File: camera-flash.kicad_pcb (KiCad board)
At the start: 2 copper layers, 100 x 95.8 mm, 94 parts, among them J1 USB, J10 CAM, J11 GND, J2 LED_WW_A, J3 LED_WW_C, J4 LED_CW_A, J5 LED_CW_C, J6 IN, J7 OUT, J8 CAM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

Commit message: routing 50% done"
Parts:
- D1, D2, D5: footprint Diode_SMD:D_SMA -> Diode_SMD:D_SOD-123F
- Q1, Q2: value 2N7002 -> ONSC-NMOS-8_E; footprint Package_TO_SOT_SMD:SOT-23 -> Package_SO:SO-8_3.9x4.9mm_P1.27mm
- R10, R9: footprint otter:R_0603 -> otter:R_0805
- moved C19 204.0 mm to (119.9, 126.8), turned to 90 degrees
- moved R27 203.2 mm to (135.4, 100.3), turned to 225 degrees
- moved C20 202.8 mm to (137.3, 106.2), turned to 270 degrees
- moved U7 198.6 mm to (132.6, 105.0)
- moved R13 193.0 mm to (113.1, 138.0), turned to 270 degrees
- moved C21 190.0 mm to (128.0, 103.7), turned to 270 degrees
- moved R16 189.6 mm to (128.1, 101.5), turned to 180 degrees
- moved R17 188.9 mm to (128.0, 106.2), turned to 270 degrees
- moved R14 187.0 mm to (120.5, 128.8), turned to 180 degrees
- moved D5 186.4 mm to (109.9, 126.8), turned to 90 degrees
- moved C23 186.0 mm to (133.7, 108.6), turned to 180 degrees
- moved R18 185.6 mm to (130.6, 108.5)
- moved C22 184.4 mm to (125.0, 123.3), turned to 90 degrees
- moved U5 183.8 mm to (115.2, 126.8), turned to 90 degrees
- moved U6 182.7 mm to (122.5, 124.3)
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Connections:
- J6 pad 1: Net-(D5-Pad2) -> Net-(J6-Pad1)
- J6 pad 2: Net-(J6-Pad2) -> Net-(D5-Pad2)
- Q1 pad 1: Net-(Q1-Pad1) -> Net-(C17-Pad1)
- Q1 pad 3: Net-(C17-Pad2) -> Net-(C17-Pad1)
- Q2 pad 1: Net-(Q2-Pad1) -> Net-(C18-Pad1)
- Q2 pad 3: Net-(C18-Pad2) -> Net-(C18-Pad1)
- R12 pad 2: WW_DIM -> CW_DIM
- R13 pad 2: Net-(J6-Pad2) -> Net-(J6-Pad1)
- R19 pad 1: Net-(Q1-Pad1) -> Net-(Q1-Pad4)
- R20 pad 1: Net-(Q2-Pad1) -> Net-(Q2-Pad4)
- R8 pad 1: WW_DIM -> CW_DIM
- U4 pad 6: WW_DIM -> CW_DIM
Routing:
- net CC2: track 0.00 -> 4.70 mm
- net CC1: track 0.00 -> 4.28 mm
- added copper zone on B.Cu, net GND
- added copper zone on F.Cu, net GND

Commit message: update
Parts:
- moved D1 102.5 mm to (126.3, 62.6), turned to 135 degrees
- moved R19 90.2 mm to (123.0, 59.5), turned to 135 degrees
- moved C24 89.5 mm to (101.5, 55.5)
- moved Q3 89.1 mm to (101.5, 53.0), turned to 180 degrees
- moved R23 85.7 mm to (98.5, 53.5), turned to 180 degrees
- moved Q7 85.6 mm to (95.5, 53.5), turned to 90 degrees
- moved R21 85.4 mm to (98.5, 52.0), turned to 180 degrees
- moved Q4 77.1 mm to (105.0, 53.0), turned to 270 degrees
- moved D2 74.3 mm to (72.0, 106.0), turned to 90 degrees
- moved R25 69.4 mm to (98.5, 55.0)
- moved C25 48.8 mm to (74.0, 94.1), turned to 90 degrees
- moved Q5 45.4 mm to (72.3, 97.4), turned to 90 degrees
- moved C12 45.1 mm to (61.3, 116.0), turned to 270 degrees
- moved R24 40.1 mm to (72.4, 94.4), turned to 90 degrees
- moved R20 39.3 mm to (70.5, 100.8), turned to 90 degrees
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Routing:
- net +3V3: track 0.00 -> 234.3 mm, vias 0 -> 6
- net Net-(C17-Pad2): track 0.00 -> 26.5 mm
- net Net-(C18-Pad2): track 0.00 -> 25.3 mm
- net Net-(D5-Pad2): track 0.00 -> 23.4 mm
- net Net-(C18-Pad1): track 0.00 -> 22.3 mm
- net VBUS: track 0.00 -> 18.9 mm, vias 0 -> 15
- net GND: track 0.00 -> 16.3 mm
- net Net-(D5-Pad1): track 0.00 -> 12.7 mm
- net Net-(SW3-Pad3): track 0.00 -> 12.6 mm
- net Net-(SW2-Pad2): track 0.00 -> 12.2 mm
- net Net-(C17-Pad1): track 0.00 -> 11.5 mm
- net Net-(R14-Pad1): track 0.00 -> 10.7 mm
- net Net-(SW3-Pad2): track 0.00 -> 8.27 mm
- net flash_in: track 0.00 -> 8.14 mm
- net Net-(R15-Pad1): track 0.00 -> 7.65 mm
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- added copper zone on B.Cu, net Net-(C13-Pad1)
- added copper zone on B.Cu, net Net-(C14-Pad1)
- added copper zone on B.Cu, net Net-(C17-Pad1)
- added copper zone on B.Cu, net Net-(C17-Pad2)
- added copper zone on B.Cu, net Net-(C18-Pad1)
- added copper zone on B.Cu, net Net-(C18-Pad2)
- added copper zone on B.Cu, net VBUS
- added copper zone on F.Cu, net VBUS
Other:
- rule pad_to_mask_clearance: 0.051 -> 0

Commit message: update
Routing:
- net VBUS: track 18.9 -> 244.8 mm, vias 15 -> 30
- net flash_pulse: track 3.29 -> 172.9 mm, vias 0 -> 9
- net flash_in: track 8.14 -> 71.4 mm, vias 0 -> 6
- net +3V3: track 234.3 -> 295.7 mm, vias 6 -> 10
- net Net-(R12-Pad1): track 0.00 -> 42.7 mm, vias 0 -> 2
- net Net-(Q3-Pad2): track 0.00 -> 23.5 mm
- net Net-(R11-Pad1): track 0.00 -> 12.1 mm, vias 0 -> 2
- net Net-(R15-Pad1): track 7.65 -> 14.1 mm, vias 0 -> 2
- net Net-(Q7-Pad3): track 0.00 -> 6.12 mm
- net Net-(Q3-Pad1): track 0.00 -> 4.80 mm
- net Net-(Q5-Pad2): track 3.06 -> 6.24 mm
- net Net-(Q1-Pad4): track 0.00 -> 2.39 mm
- net Net-(Q8-Pad1): track 6.64 -> 4.32 mm
- net Net-(Q5-Pad1): track 5.14 -> 7.41 mm
- net Net-(Q7-Pad1): track 0.00 -> 1.51 mm
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
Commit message: update
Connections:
- J1 pad A6: D+ -> Net-(J1-PadA6)
- J1 pad A7: D- -> Net-(J1-PadA7)
- J1 pad B6: D+ -> Net-(J1-PadB6)
- J1 pad B7: D- -> Net-(J1-PadB7)
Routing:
- net GND: vias 7 -> 135
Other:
- net class Default: clearance 0.2 -> 0.19
- rule trace_clearance: 0.2 -> 0.19

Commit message: update
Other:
- board text added: "CW"
- board text added: "DELAY"
- board text added: "DELAYED DIRECT"
- board text added: "IN - +"
- board text added: "OFF ON"
- board text added: "OUT + -"
- board text added: "OUTPUT"
- board text added: "T-ON"
- board text added: "TRIGGER"
- board text added: "WW"
- board text added: "↑ ↓"
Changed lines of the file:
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@@
   (general
     (thickness 1.6)
-    (drawings 9)
+    (drawings 29)
     (tracks 709)
     (zones 0)
@@
     (pcbplotparams
       (layerselection 0x010fc_ffffffff)
-      (usegerberextensions false)
+      (usegerberextensions true)
       (usegerberattributes false)
       (usegerberadvancedattributes false)
@@
       (psa4output false)
       (plotreference true)
-      (plotvalue true)
+      (plotvalue false)
       (plotinvisibletext false)
       (padsonsilk false)
@@
       (outputformat 1)
       (mirror false)
-      (drillshape 1)
+      (drillshape 0)
       (scaleselection 1)
-      (outputdirectory ""))
+      (outputdirectory "gerber/"))
   )
   (net 0 "")
@@
     )
   )
+  (gr_line (start 114.4 141.6) (end 110.6 141.6) (layer F.SilkS) (width 0.12))
+  (gr_line (start 110.6 145.4) (end 114.4 145.4) (layer F.SilkS) (width 0.12))
+  (gr_line (start 110.6 141.6) (end 110.6 145.4) (layer F.SilkS) (width 0.12))
+  (gr_line (start 114.4 145.4) (end 114.4 141.6) (layer F.SilkS) (width 0.12))
+  (gr_line (start 89.4 141.6) (end 85.6 141.6) (layer F.SilkS) (width 0.12))
+  (gr_line (start 89.4 145.4) (end 89.4 141.6) (layer F.SilkS) (width 0.12))
+  (gr_line (start 85.6 145.4) (end 89.4 145.4) (layer F.SilkS) (width 0.12))
+  (gr_line (start 85.6 141.6) (end 85.6 145.4) (layer F.SilkS) (width 0.12))
+  (gr_text "DELAYED  DIRECT\n" (at 88 137.8) (layer F.SilkS)
+    (effects (font (size 0.8 0.8) (thickness 0.15)))
+  )
+  (gr_text OUTPUT (at 88.2 131.4) (layer F.SilkS)
+    (effects (font (size 1 1) (thickness 0.15)))
+  )
+  (gr_text CW (at 71.4 64.8) (layer F.SilkS)
+    (effects (font (size 1 1) (thickness 0.15)))
+  )
+  (gr_text "WW\n" (at 134.2 79.8) (layer F.SilkS)
+    (effects (font (size 1 1) (thickness 0.15)))
+  )
+  (gr_text T-ON (at 130 86.2) (layer F.SilkS)
+    (effects (font (size 1 1) (thickness 0.15)))
+  )
+  (gr_text DELAY (at 140.6 106.6) (layer F.SilkS)
+    (effects (font (size 1 1) (thickness 0.15)))
+  )
+  (gr_text "↑   ↓" (at 131.8 129.4) (layer F.SilkS)
+    (effects (font (size 1 1) (thickness 0.15)))
+  )
+  (gr_text "OFF ON" (at 142 101) (layer F.SilkS)
+    (effects (font (size 1 1) (thickness 0.15)))
+  )
+  (gr_text DELAY (at 142 94.8) (layer F.SilkS)
+    (effects (font (size 1 1) (thickness 0.15)))
+  )
+  (gr_text TRIGGER (at 131.8 123.2) (layer F.SilkS)
+    (effects (font (size 1 1) (thickness 0.15)))
+  )
+  (gr_text "OUT\n+ -" (at 87.4 143.5) (layer F.SilkS)
+    (effects (font (size 1 1) (thickness 0.15)))
+  )
+  (gr_text "IN\n- +" (at 112.4 143.5) (layer F.SilkS)
+    (effects (font (size 1 1) (thickness 0.15)))
+  )
   (gr_line (start 100 136) (end 100 126.1) (layer Eco2.User) (width 0.15))
   (gr_text "PD OK\n" (at 99.3 128) (layer F.SilkS)
@@
   (gr_line (start 120.06 145.8) (end 79.94 145.8) (layer Edge.Cuts) (width 0.05))
   (gr_circle (center 100 100) (end 125 100) (layer Edge.Cuts) (width 0.05))
+  (segment (start 102.95 131.4) (end 103.45 131.4) (width 0.2) (layer B.Cu) (net 1))
+  (segment (start 102.8 131.55) (end 102.95 131.4) (width 0.2) (layer B.Cu) (net 1))
+  (segment (start 102.8 132.325) (end 102.8 131.55) (width 0.2) (layer B.Cu) (net 1))
+  (segment (start 102.575 132.55) (end 102.8 132.325) (width 0.2) (layer B.Cu) (net 1))
+  (segment (start 101.9625 132.55) (end 102.575 132.55) (width 0.2) (layer B.Cu) (net 1))
   (via (at 116.25 70.75) (size 0.6) (drill 0.3) (layers F.Cu B.Cu) (net 2))
   (via (at 110.25 133) (size 0.6) (drill 0.3) (layers F.Cu B.Cu) (net 2))
@@
   (via (at 100.75 133.5) (size 0.6) (drill 0.3) (layers F.Cu B.Cu) (net 2))
   (via (at 100.75 132) (size 0.6) (drill 0.3) (layers F.Cu B.Cu) (net 2))
-  (via (at 102.1 137.1) (size 0.6) (drill 0.3) (layers F.Cu B.Cu) (net 5))
-  (via (at 102.1 136.4) (size 0.6) (drill 0.3) (layers F.Cu B.Cu) (net 5))
-  (segment (start 102.95 131.4) (end 103.45 131.4) (width 0.2) (layer B.Cu) (net 1))
-  (segment (start 102.8 131.55) (end 102.95 131.4) (width 0.2) (layer B.Cu) (net 1))
-  (segment (start 102.8 132.325) (end 102.8 131.55) (width 0.2) (layer B.Cu) (net 1))
-  (segment (start 102.575 132.55) (end 102.8 132.325) (width 0.2) (layer B.Cu) (net 1))
-  (segment (start 101.9625 132.55) (end 102.575 132.55) (width 0.2) (layer B.Cu) (net 1))
   (segment (start 114.927565 68.177565) (end 114.927565 69.322435) (width 0.25) (layer B.Cu) (net 2))
   (segment (start 114.132159 67.382159) (end 114.927565 68.177565) (width 0.25) (layer B.Cu) (net 2))
@@
   (segment (start 72 110) (end 73.75 108.25) (width 0.2) (layer B.Cu) (net 4))
   (segment (start 66.5 119.25) (end 66.625 119.25) (width 0.2) (layer B.Cu) (net 4))
+  (via (at 102.1 137.1) (size 0.6) (drill 0.3) (layers F.Cu B.Cu) (net 5))
+  (via (at 102.1 136.4) (size 0.6) (drill 0.3) (layers F.Cu B.Cu) (net 5))
   (segment (start 116.447845 73.508505) (end 117.56967 74.63033) (width 0.25) (layer B.Cu) (net 5))
   (segment (start 116.447845 73.392566) (end 116.447845 73.508505) (width 0.25) (layer B.Cu) (net 5))

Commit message: finished layout
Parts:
- moved RV2 4.28 mm to (74.1, 73.3)
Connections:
- RV2 pad 1: Net-(RV2-Pad1) -> +3V3
- RV2 pad 2: +3V3 -> Net-(R12-Pad1)
- RV2 pad 3: Net-(R12-Pad1) -> Net-(RV2-Pad3)
- RV4 pad 2: +3V3 -> Net-(R16-Pad1)
- RV4 pad 3: Net-(R16-Pad1) -> +3V3
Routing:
- net +3V3: track 295.7 -> 242.8 mm
- net VBUS: track 244.8 -> 271.5 mm
- net Net-(R11-Pad1): track 12.1 -> 14.9 mm
- net Net-(R12-Pad1): track 42.7 -> 43.9 mm
- net Net-(R15-Pad1): track 14.1 -> 13.1 mm, vias 2 -> 0
- net GND: vias 135 -> 137
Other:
- board text added: "+ -"
- board text added: "BRIGHTNESS CW"
- board text added: "BRIGHTNESS WW"
- board text added: "Jan Henrik 2020"
- board text added: "Zoetrope -Flash"
- board text added: "t-ON"
- board text removed: "CW"
- board text removed: "T-ON"
- board text removed: "WW"

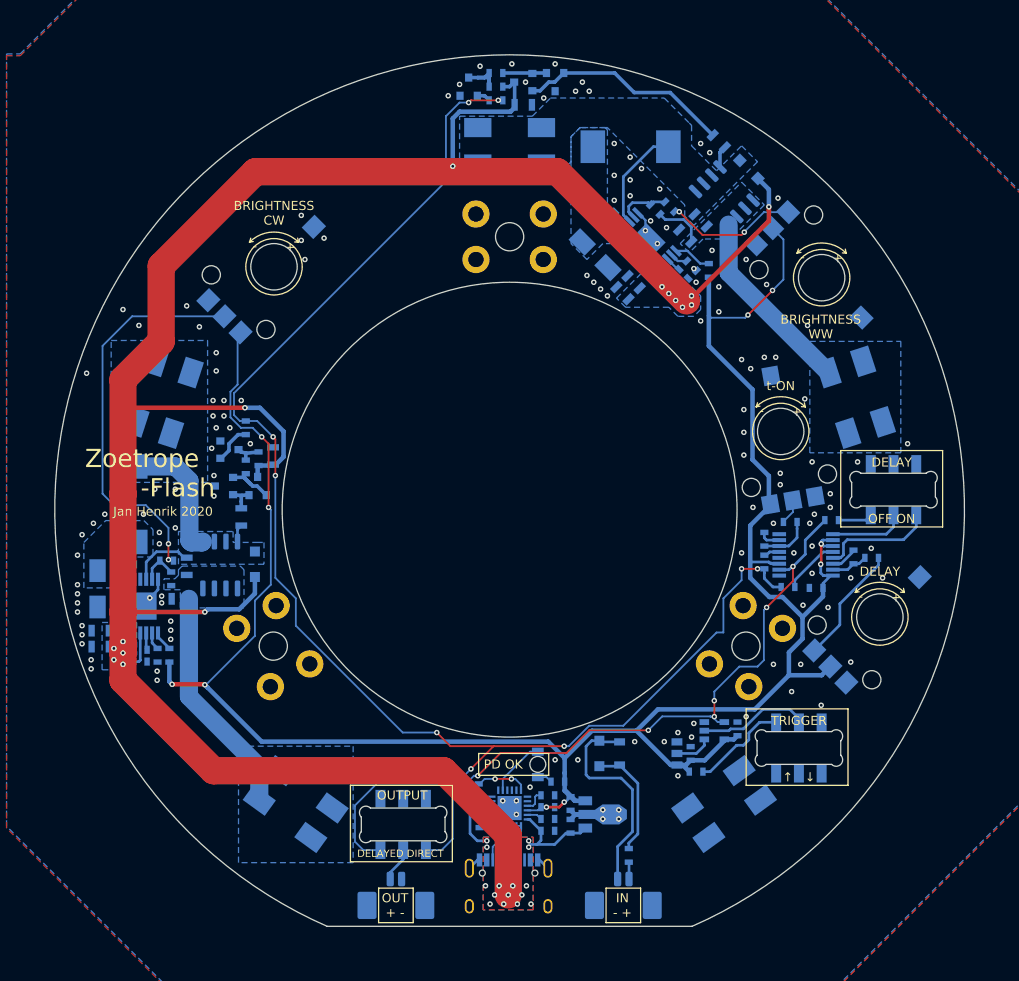
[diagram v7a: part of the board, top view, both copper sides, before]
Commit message: updated to kicad 6
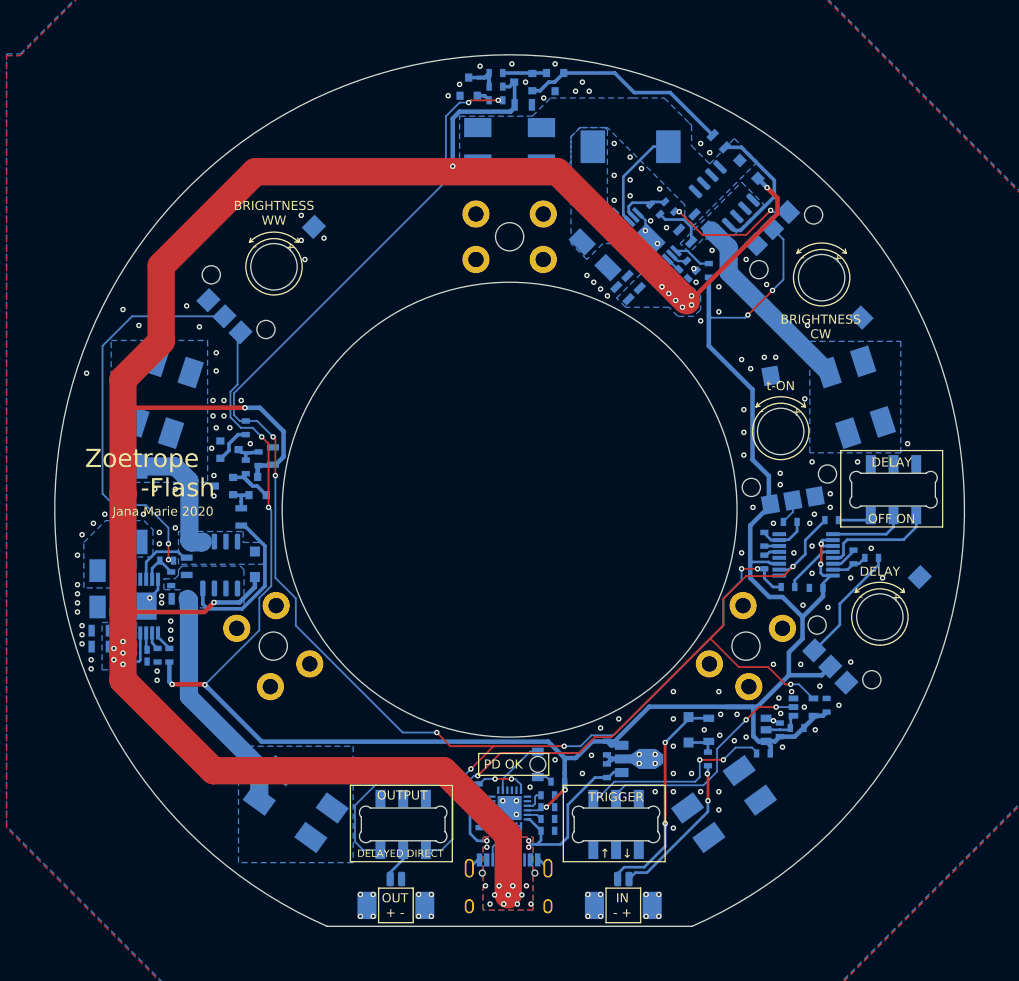
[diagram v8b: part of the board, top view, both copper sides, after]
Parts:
- added R29: 10k, otter:R_0603, B.Cu at (131.6, 124.0)
- C20, C21: value C_Small -> 470n
- R10, R9: value R_Small -> 0.4
- R11, R12: value 150k -> 15k
- R15, R16: value 150k -> 100
- R17: value DNP -> 0
- R18: value 0 -> DNP
- moved SW2 21.8 mm to (111.7, 134.6)
- moved R13 13.7 mm to (121.8, 127.4)
- moved D5 10.1 mm to (119.7, 124.2)
- moved U6 10.1 mm to (132.3, 121.7)
- moved C22 10.1 mm to (134.8, 121.5)
- moved U5 10.1 mm to (125.0, 124.2)
- moved C19 10.1 mm to (129.7, 124.2)
- moved R14 7.67 mm to (127.9, 126.8), turned to 0 degrees
- moved C5 7.29 mm to (110.7, 128.7)
- moved C6 7.29 mm to (110.7, 126.2)
- moved U2 7.29 mm to (113.8, 127.4)
- turned C21 to 90 degrees
- turned Q1 to 135 degrees
- turned Q2 to 90 degrees
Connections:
- Q1 pad 1: Net-(C17-Pad1) -> Net-(C17-Pad2)
- Q1 pad 2: Net-(C17-Pad1) -> Net-(C17-Pad2)
- Q1 pad 3: Net-(C17-Pad1) -> Net-(C17-Pad2)
- Q1 pad 5: Net-(C17-Pad2) -> Net-(C17-Pad1)
- Q1 pad 6: Net-(C17-Pad2) -> Net-(C17-Pad1)
- Q1 pad 7: Net-(C17-Pad2) -> Net-(C17-Pad1)
- Q1 pad 8: Net-(C17-Pad2) -> Net-(C17-Pad1)
- Q2 pad 1: Net-(C18-Pad1) -> Net-(C18-Pad2)
- Q2 pad 2: Net-(C18-Pad1) -> Net-(C18-Pad2)
- Q2 pad 3: Net-(C18-Pad1) -> Net-(C18-Pad2)
- Q2 pad 5: Net-(C18-Pad2) -> Net-(C18-Pad1)
- Q2 pad 6: Net-(C18-Pad2) -> Net-(C18-Pad1)
- Q2 pad 7: Net-(C18-Pad2) -> Net-(C18-Pad1)
- Q2 pad 8: Net-(C18-Pad2) -> Net-(C18-Pad1)
- U7 pad 6: Net-(C21-Pad2) -> Net-(C21-Pad1)
- U7 pad 7: Net-(C21-Pad1) -> Net-(C21-Pad2)
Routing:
- net Net-(Q2-Pad4): track 1.93 -> 17.7 mm
- net Net-(J6-Pad1): track 1.86 -> 16.8 mm, vias 0 -> 2
- net Net-(SW2-Pad2): track 12.2 -> 25.4 mm, vias 0 -> 2
- net Net-(Q1-Pad4): track 2.39 -> 15.6 mm
- net Net-(R14-Pad1): track 10.7 -> 22.4 mm, vias 0 -> 2
- net Net-(D5-Pad1): track 12.7 -> 3.45 mm
- net VBUS: track 271.5 -> 280.6 mm
- net flash_in: track 71.4 -> 80.2 mm, vias 6 -> 3
- net +3V3: track 242.8 -> 240.7 mm
- net Net-(D5-Pad2): track 23.4 -> 24.6 mm, vias 0 -> 2
- net Net-(C21-Pad1): track 2.34 -> 1.64 mm
- net GND: vias 137 -> 173
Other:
- net class Default removed
- board text added: "Jana Marie 2020"
- board text removed: "Jan Henrik 2020"
